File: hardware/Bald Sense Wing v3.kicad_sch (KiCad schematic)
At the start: 39 parts, among them J1 feather long, J2 feather short, J3 1140084168, Q1 Q_PNP_BEC, Q2 Q_NPN_BEC, U1 APDS-9960, U2 DS3231MZ, U3 SHT30-DIS, U4 MIC5504-3.3YM5, U5 CMM-4737DT-26186-TR

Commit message: re-worked pinout to match m0 lora feather
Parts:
- added J4: STEMMA-QT, symbol Connector_Generic:Conn_01x04
- D1: symbol Device:LED_Small_ALT -> Device:LED_Small_Filled
- JP2: symbol freetronics_schematic:M02 -> Connector_Generic:Conn_01x02
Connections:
- net AREF is gone; now on net 3v3_feather: J1.14 (Pin_14)
- net +3.3V: now also JP2.1 (Pin_1), J4.3 (Pin_3)
- net APDS_INT: now also J1.9 (Pin_9); no longer J1.7 (Pin_7)
- net Batt_Meas: now also J1.11 (Pin_11); no longer J1.8 (Pin_8)
- net Batt_Meas_En: now also J1.10 (Pin_10); no longer J1.9 (Pin_9)
- net GND: now also D1.1 (K), J4.4 (Pin_4)
- net SCL: now also J4.1 (Pin_1)
- net SDA: now also J4.2 (Pin_2)
- net SD_CD: now also J1.8 (Pin_8); no longer J1.12 (Pin_12)
- net SD_CS: now also J1.7 (Pin_7); no longer J1.11 (Pin_11)
- net VUSB_Meas: now also J1.12 (Pin_12); no longer J1.10 (Pin_10)
- net at R11.1: now also D1.2 (A)
- net at JP4.1 (A), U4.5 (VOUT): now also JP2.2 (Pin_2)
- no-connect marks 0 -> 2
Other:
- note added: "- Temp / Humidity: SHT30-DIS-B2.5KS - Light: APDS9960 - Sound: MP34DT01TR-M - RTC: DS3231S - Coin Cell Holder CR2032 - Micro SD Card Socket - Stemma QT Socket (NEED TO ADD)"
- note added: "3v3 Regulator"
- note added: "DS3231 Real-Time Clock (RTC)"
- note added: "SHT30 Temperature and Humidity"
- note added: "TODO: Change to load switch"
- note removed: "- Temp / Humidity: SHT30-DIS-B2.5KS - Light: APDS9960 - Sound: MP34DT01TR-M - RTC: DS3231S - Coin Cell Holder CR2032 - Micro SD Card Socket"
- note removed: "DS3231 RTC"
- note removed: "On-board 3.3v regulator"
- note removed: "SHT30 - Temperature and Humidity"
- note removed: "TODO: Verify MicroSD Card Pin Out. (can we use QPSI or SDIO?)"

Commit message: removed LDO and unconnected a few pins to be compatible with feathers3
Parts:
- removed C5, C6: 1uF, Capacitor_SMD:C_0805_2012Metric, symbol Device:C_Small
- removed JP2: M02, Connector_PinHeader_2.54mm:PinHeader_1x02_P2.54mm_Vertical, symbol Connector_Generic:Conn_01x02
- removed JP4: Reg En, Jumper:SolderJumper-2_P1.3mm_Bridged_RoundedPad1.0x1.5mm, symbol Jumper:SolderJumper_2_Bridged
- removed R4: DNP, Resistor_SMD:R_0805_2012Metric, symbol Device:R_Small
- removed U4: MIC5504-3.3YM5, Package_TO_SOT_SMD:SOT-23-5, symbol Regulator_Linear:MIC5504-3.3YM5
- added TP1, TP2, TP3, TP4, TP5, TP6: TestPoint_Harwin, My Libraries:Harwin-S1751-46-Test-Point, symbol My Library:TestPoint_Harwin
- J3: Field8 (none) -> MicroSD Card Socket
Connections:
- net 3v3_feather: no longer J1.14 (Pin_14)
- net Batt_Meas: now also TP5.1
- net RX: now also TP2.1
- net TX: now also TP3.1
- net VUSB_Meas: now also TP6.1
- net 3v3_Reg_En renamed Load_SW_En
- net FREE renamed NC1
- net NC1: now also TP4.1
- new net NC2: J1.14 (Pin_14), TP1.1
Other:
- note added: "Load Switch Bypass"
- note added: "Load Switch for Sensors"
- note removed: "3v3 Regulator"

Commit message: changed R to 0402 and C to 0603
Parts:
- C1, C2, C3, C4, C7: footprint Capacitor_SMD:C_0805_2012Metric -> Capacitor_SMD:C_0603_1608Metric
- D1: footprint LED_SMD:LED_1206_3216Metric -> LED_SMD:LED_0805_2012Metric
- R1, R10, R11, R12, R13, R14, R2, R3, R5, R6, R7, R8, R9: footprint Resistor_SMD:R_0805_2012Metric -> Resistor_SMD:R_0402_1005Metric
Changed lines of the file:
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@@
 			)
 		)
-		(property "Footprint" "Resistor_SMD:R_0805_2012Metric"
+		(property "Footprint" "Resistor_SMD:R_0402_1005Metric"
 			(at 184.15 148.59 0)
 			(effects
@@
 			)
 		)
-		(property "Footprint" "Resistor_SMD:R_0805_2012Metric"
+		(property "Footprint" "Resistor_SMD:R_0402_1005Metric"
 			(at 176.53 148.59 0)
 			(effects
@@
 			)
 		)
-		(property "Footprint" "Resistor_SMD:R_0805_2012Metric"
+		(property "Footprint" "Resistor_SMD:R_0402_1005Metric"
 			(at 68.58 35.56 0)
 			(effects
@@
 			)
 		)
-		(property "Footprint" "Resistor_SMD:R_0805_2012Metric"
+		(property "Footprint" "Resistor_SMD:R_0402_1005Metric"
 			(at 76.2 35.56 0)
 			(effects
@@
 			)
 		)
-		(property "Footprint" "Capacitor_SMD:C_0805_2012Metric"
+		(property "Footprint" "Capacitor_SMD:C_0603_1608Metric"
 			(at 29.21 30.48 0)
 			(effects
@@
 			)
 		)
-		(property "Footprint" "Capacitor_SMD:C_0805_2012Metric"
+		(property "Footprint" "Capacitor_SMD:C_0603_1608Metric"
 			(at 153.67 29.21 0)
 			(effects
@@
 			)
 		)
-		(property "Footprint" "Capacitor_SMD:C_0805_2012Metric"
+		(property "Footprint" "Capacitor_SMD:C_0603_1608Metric"
 			(at 92.71 39.37 0)
 			(effects
@@
 			)
 		)
-		(property "Footprint" "Capacitor_SMD:C_0805_2012Metric"
+		(property "Footprint" "Capacitor_SMD:C_0603_1608Metric"
 			(at 26.67 90.17 0)
 			(effects
@@
 			)
 		)
-		(property "Footprint" "Resistor_SMD:R_0805_2012Metric"
+		(property "Footprint" "Resistor_SMD:R_0402_1005Metric"
 			(at 44.45 87.63 0)
 			(effects
@@
 			)
 		)
-		(property "Footprint" "Resistor_SMD:R_0805_2012Metric"
+		(property "Footprint" "Resistor_SMD:R_0402_1005Metric"
 			(at 157.48 147.32 0)
 			(effects
@@
 			)
 		)
-		(property "Footprint" "LED_SMD:LED_1206_3216Metric"
+		(property "Footprint" "LED_SMD:LED_0805_2012Metric"
 			(at 165.1 147.32 90)
 			(effects
@@
 			)
 		)
-		(property "Footprint" "Capacitor_SMD:C_0805_2012Metric"
+		(property "Footprint" "Capacitor_SMD:C_0603_1608Metric"
 			(at 107.95 154.94 0)
 			(effects
@@
 			)
 		)
-		(property "Footprint" "Resistor_SMD:R_0805_2012Metric"
+		(property "Footprint" "Resistor_SMD:R_0402_1005Metric"
 			(at 241.3 101.6 0)
 			(effects
@@
 			)
 		)
-		(property "Footprint" "Resistor_SMD:R_0805_2012Metric"
+		(property "Footprint" "Resistor_SMD:R_0402_1005Metric"
 			(at 241.3 111.76 0)
 			(effects
@@
 			)
 		)
-		(property "Footprint" "Resistor_SMD:R_0805_2012Metric"
+		(property "Footprint" "Resistor_SMD:R_0402_1005Metric"
 			(at 219.71 139.7 0)
 			(effects
@@
 			)
 		)
-		(property "Footprint" "Resistor_SMD:R_0805_2012Metric"
+		(property "Footprint" "Resistor_SMD:R_0402_1005Metric"
 			(at 234.95 130.81 0)
 			(effects
@@
 			)
 		)
-		(property "Footprint" "Resistor_SMD:R_0805_2012Metric"
+		(property "Footprint" "Resistor_SMD:R_0402_1005Metric"
 			(at 251.46 144.78 0)
 			(effects
@@
 			)
 		)
-		(property "Footprint" "Resistor_SMD:R_0805_2012Metric"
+		(property "Footprint" "Resistor_SMD:R_0402_1005Metric"
 			(at 251.46 153.67 0)
 			(effects
@@
 			)
 		)
-		(property "Footprint" "Resistor_SMD:R_0805_2012Metric"
+		(property "Footprint" "Resistor_SMD:R_0402_1005Metric"
 			(at 241.3 134.62 0)
 			(effects

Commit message: Cleaned up older custom symbols. Ran track clean-up on PCB.
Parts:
- J3: footprint My Libraries:AMPHENOL_1140084168 -> AMPHENOL_1140084168
- U1: footprint My Libraries:APDS-9960 -> APDS-9960
- U3: footprint My Libraries:DFN250X250X100-9N -> DFN250X250X100-9N
- U5: footprint My Libraries:XDCR_CMM-4737DT-26186-TR -> XDCR_CMM-4737DT-26186-TR
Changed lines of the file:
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@@
 			)
 		)
-		(property "Footprint" "My Libraries:XDCR_CMM-4737DT-26186-TR"
+		(property "Footprint" "XDCR_CMM-4737DT-26186-TR"
 			(at 170.18 55.88 0)
 			(effects
@@
 			)
 		)
-		(property "Footprint" "My Libraries:AMPHENOL_1140084168"
+		(property "Footprint" "AMPHENOL_1140084168"
 			(at 62.23 185.42 0)
 			(effects
@@
 			)
 		)
-		(property "Datasheet" ""
+		(property "Datasheet" "A"
 			(at 86.36 176.53 0)
 			(effects
@@
 			)
 		)
-		(property "Footprint" "My Libraries:APDS-9960"
+		(property "Footprint" "APDS-9960"
 			(at 123.19 49.53 0)
 			(effects
@@
 			)
 		)
-		(property "Datasheet" ""
+		(property "Datasheet" "SEN-12005"
 			(at 123.19 52.07 0)
 			(effects
@@
 			)
 		)
-		(property "Footprint" "My Libraries:DFN250X250X100-9N"
+		(property "Footprint" "DFN250X250X100-9N"
 			(at 68.58 114.3 0)
 			(effects
@@
 			)
 		)
-		(property "Datasheet" ""
+		(property "Datasheet" "Sensirion"
 			(at 68.58 116.84 0)
 			(effects

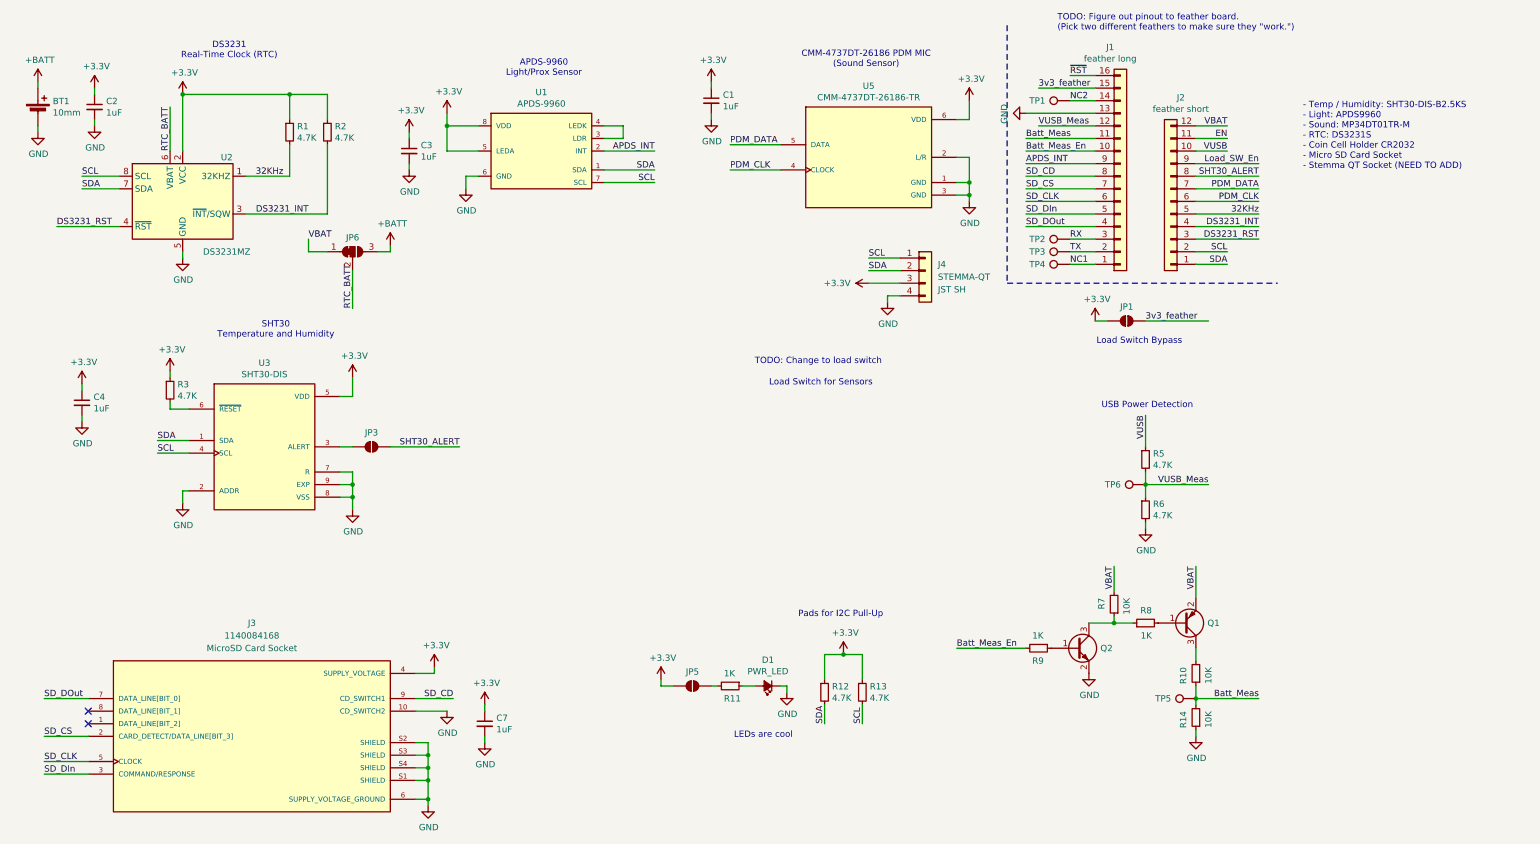
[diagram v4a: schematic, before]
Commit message: added load switch and changed power markers
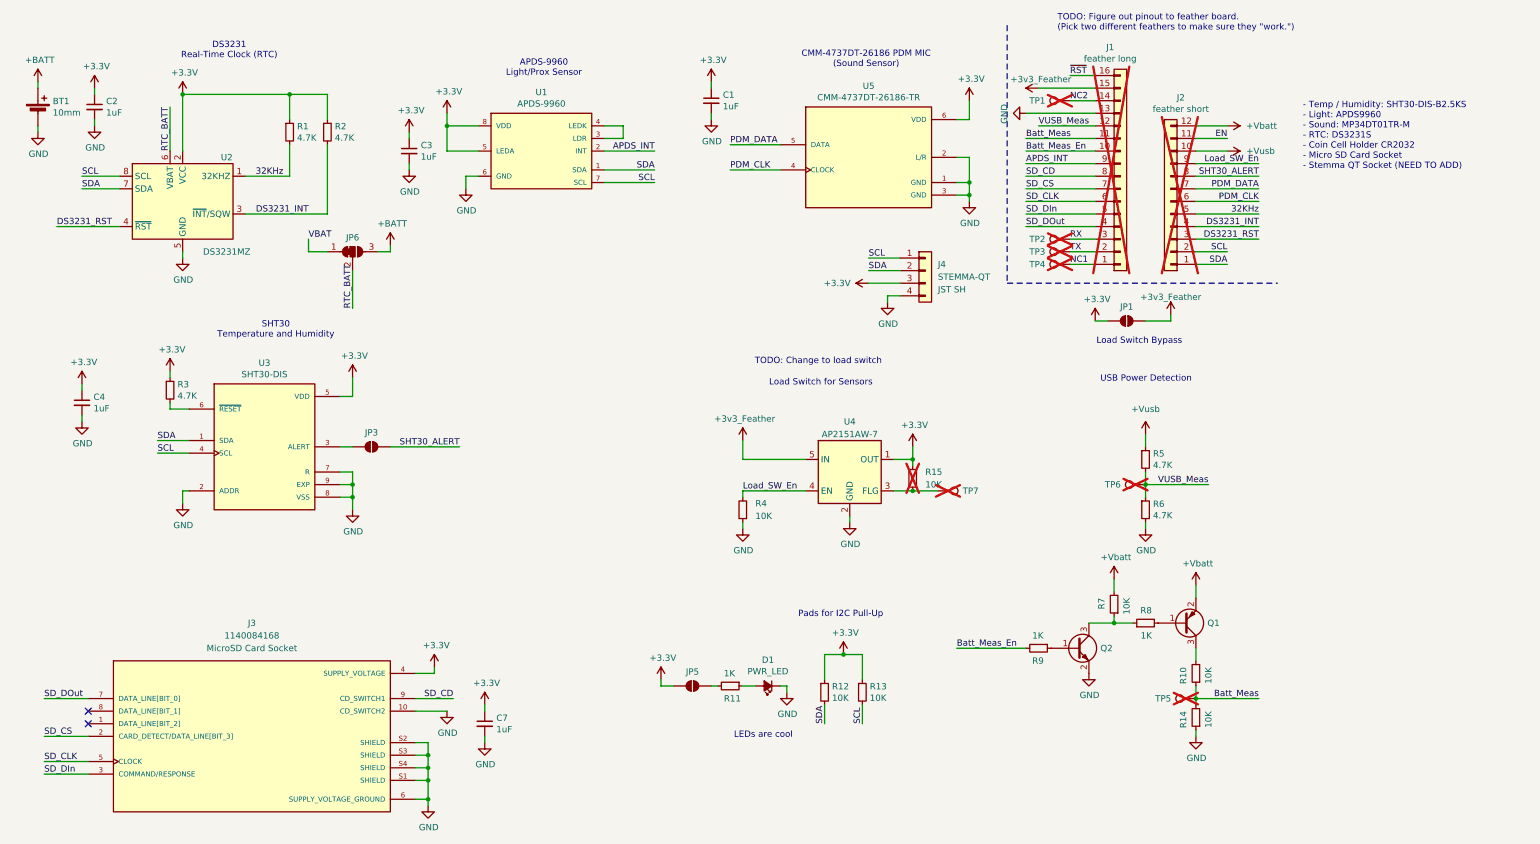
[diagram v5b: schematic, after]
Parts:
- added R15, R4: 10K, Resistor_SMD:R_0402_1005Metric, symbol Device:R_Small
- added TP7: TestPoint_Harwin, My Libraries:Harwin-S1751-46-Test-Point, symbol My Library:TestPoint_Harwin
- added U4: AP2151AW-7, Package_TO_SOT_SMD:SOT-23-5, symbol My Library:AP2151AW-7
- J1, J2, TP1, TP2, TP3, TP4, TP5, TP6: now not fitted
- R12, R13: value 4.7K -> 10K
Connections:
- net +3.3V: now also R15.2, U4.1 (OUT)
- net GND: now also R4.1, U4.2 (GND)
- net Load_SW_En: now also R4.2, U4.4 (EN)
- net VBAT: no longer J2.12 (Pin_12), Q1.2 (E), R7.2
- net 3v3_feather renamed +3v3_Feather
- net +3v3_Feather: now also U4.5 (IN)
- net VUSB renamed +Vusb
- new net: R15.1, TP7.1, U4.3 (FLG)
- new net +Vbatt: J2.12 (Pin_12), Q1.2 (E), R7.2

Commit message: re-worked pin assignments of custom packages and passed ERC
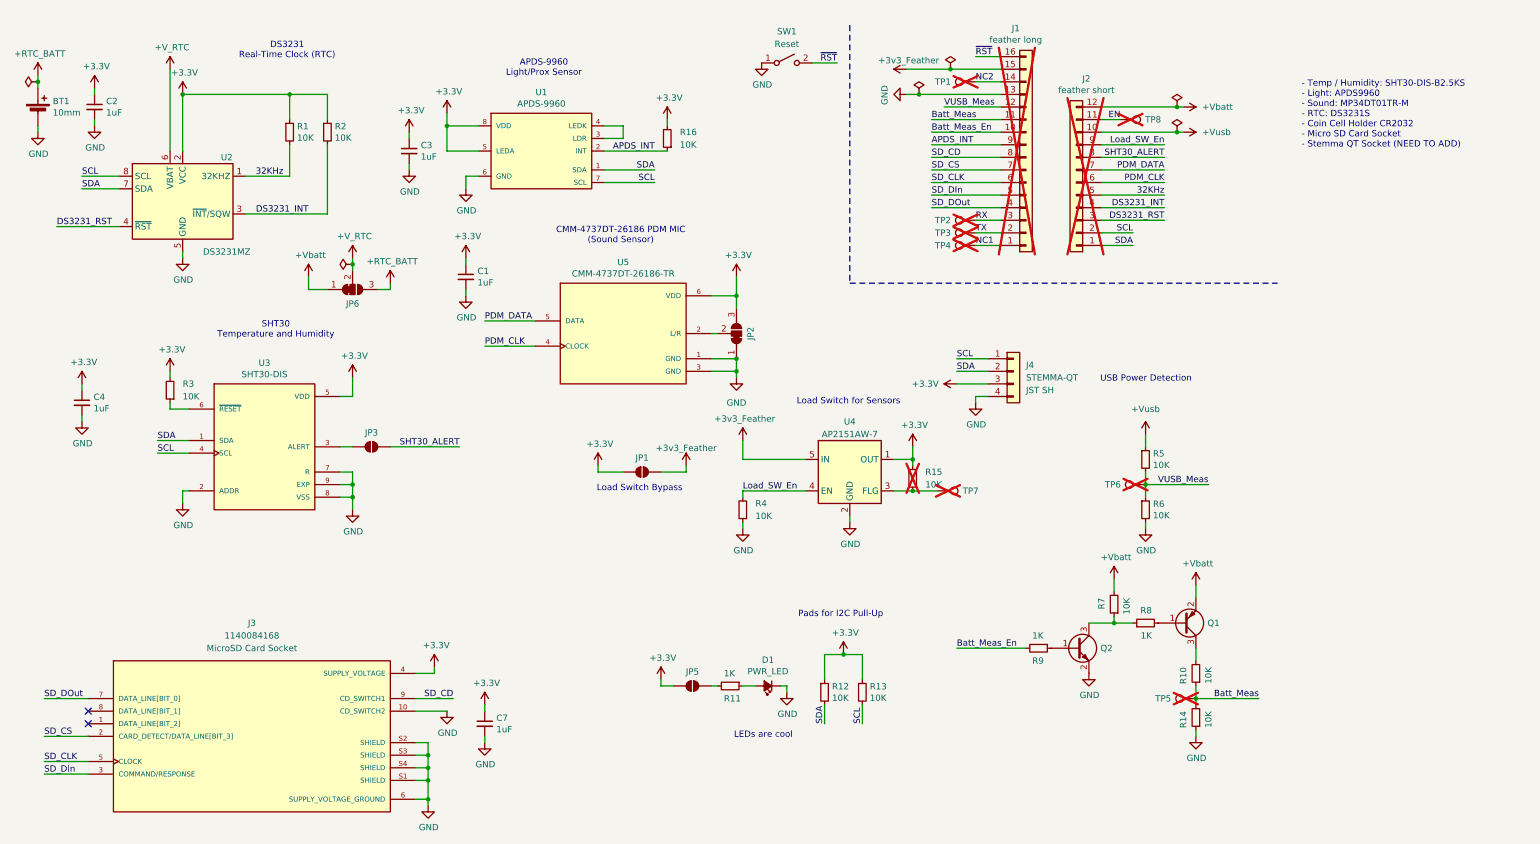
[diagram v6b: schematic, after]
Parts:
- added JP2: RTC Batt Select, Jumper:SolderJumper-3_P1.3mm_Bridged12_RoundedPad1.0x1.5mm, symbol Jumper:SolderJumper_3_Bridged12
- added R16: 10K, Resistor_SMD:R_0402_1005Metric, symbol Device:R_Small
- added SW1: Reset, symbol Switch:SW_SPST
- added TP8: TestPoint_Harwin, My Libraries:Harwin-S1751-46-Test-Point, symbol My Library:TestPoint_Harwin
- R1, R2, R3, R5, R6: value 4.7K -> 10K
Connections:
- net VBAT is gone; now on net +Vbatt: JP6.1 (A)
- net +3.3V: now also R3.2, JP2.3 (B), R16.2; no longer R3.1
- net APDS_INT: now also R16.1
- net EN: now also TP8.1
- net GND: now also JP2.1 (A), SW1.1 (A); no longer U5.2 (L/R)
- net ~{RST}: now also SW1.2 (B)
- net at U3.6 (~{RESET}): now also R3.1; no longer R3.2
- net +BATT renamed +RTC_BATT
- net RTC_BATT renamed +V_RTC
- new net: JP2.2 (C), U5.2 (L/R)
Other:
- note removed: "TODO: Change to load switch"
- note removed: "TODO: Figure out pinout to feather board. (Pick two different feathers to make sure they "work.")"
- moved on the sheet: C1, J1, J2, J4, JP1, JP6, TP1, TP2, TP3, TP4, U5

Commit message: added stemma qt connector
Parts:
- J4: footprint (none) -> Connector_JST:JST_SH_BM04B-SRSS-TB_1x04-1MP_P1.00mm_Vertical
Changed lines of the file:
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@@
 			)
 		)
-		(property "Footprint" ""
+		(property "Footprint" "Connector_JST:JST_SH_BM04B-SRSS-TB_1x04-1MP_P1.00mm_Vertical"
 			(at 214.63 83.82 0)
 			(effects
